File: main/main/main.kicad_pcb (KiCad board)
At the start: 2 copper layers, 50.8 x 76.2 mm, 1 part, among them U1 Teensy4.1

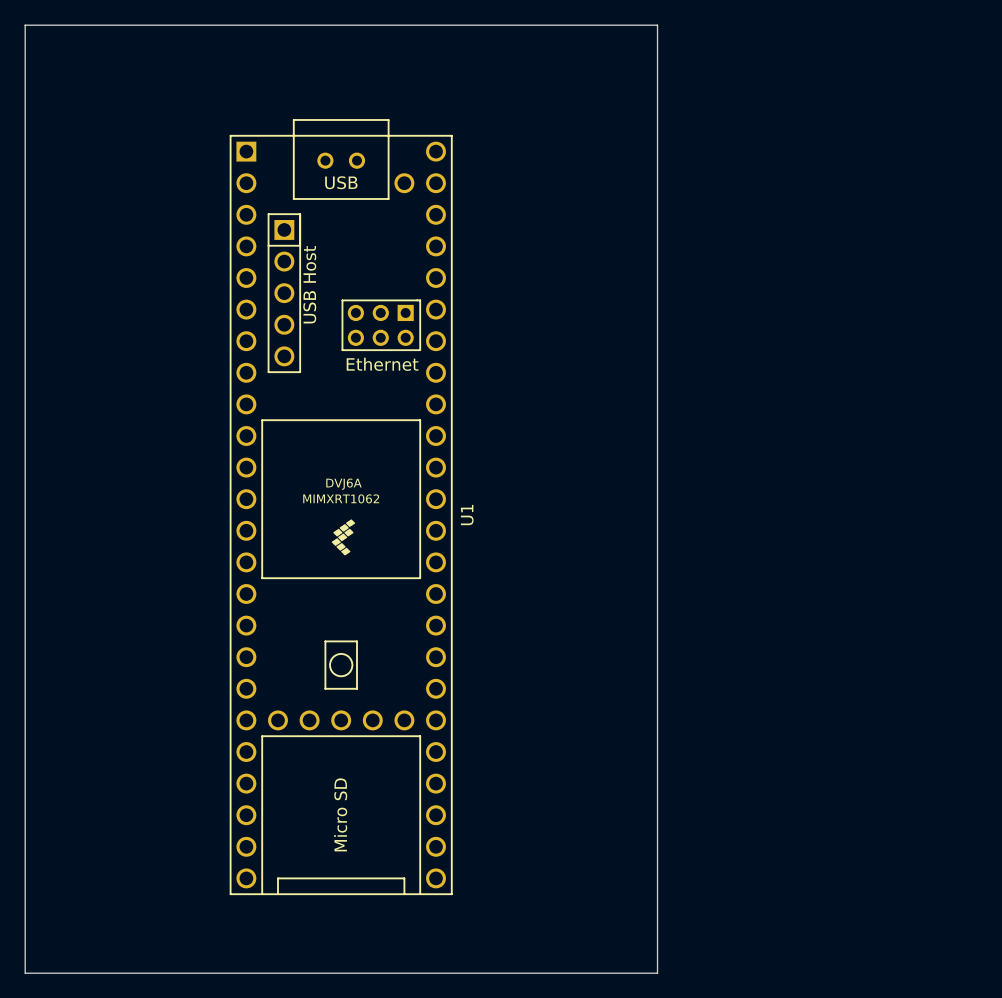
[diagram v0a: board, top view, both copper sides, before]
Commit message: working on main pcb (teensy, plugs, encoder traces)
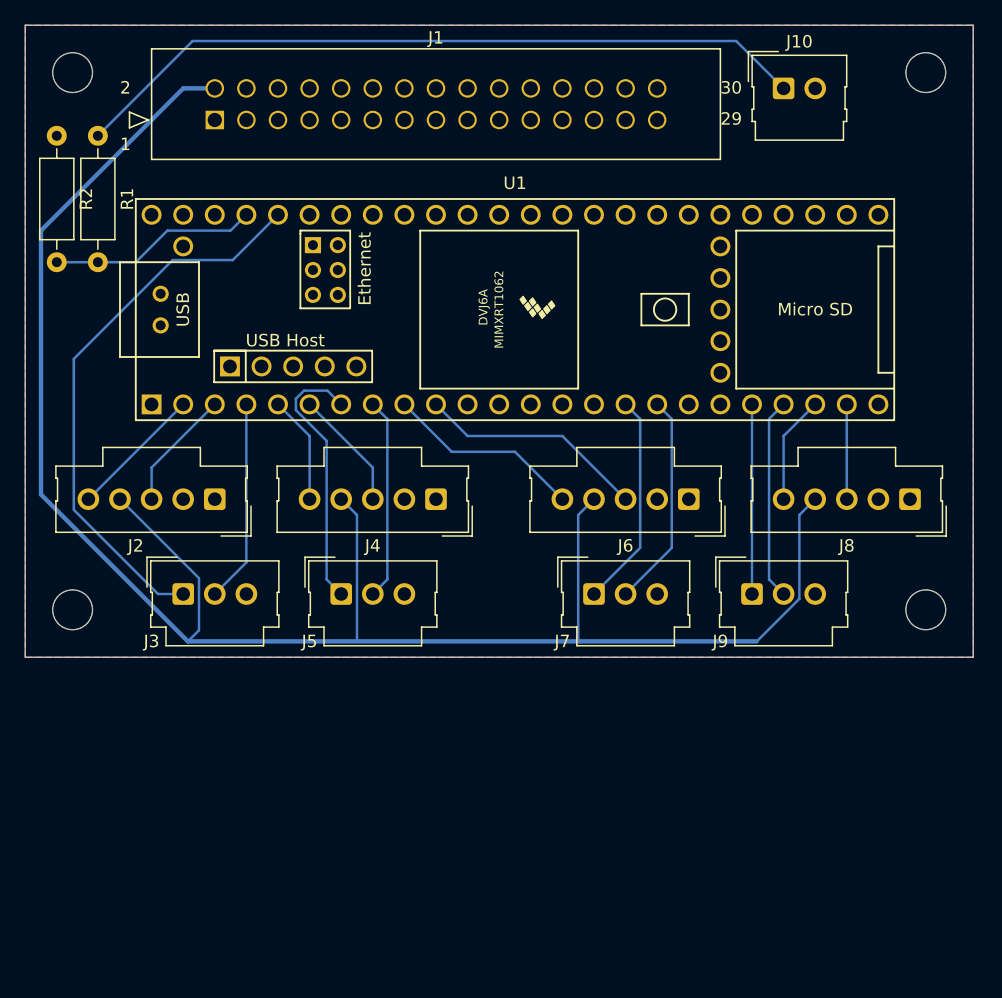
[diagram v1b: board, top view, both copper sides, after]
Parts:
- added J1: Molex2x15, projlib:CON_702463001_MOL_molex2x15, F.Cu at (116.8, 58.4)
- added J10: molex_01x02, projlib:Molex_SL_171971-0002_1x02_P2.54mm_Vertical, F.Cu at (162.6, 55.9)
- added J2: molex5P, projlib:Molex_SL_171971-0005_1x05_P2.54mm_Vertical, F.Cu at (116.8, 88.9)
- added J3: molex3P, projlib:Molex_SL_171971-0003_1x03_P2.54mm_Vertical, F.Cu at (114.3, 96.5)
- added J4: molex5P, projlib:Molex_SL_171971-0005_1x05_P2.54mm_Vertical, F.Cu at (134.6, 88.9)
- added J5: molex3P, projlib:Molex_SL_171971-0003_1x03_P2.54mm_Vertical, F.Cu at (127.0, 96.5)
- added J6: molex5P, projlib:Molex_SL_171971-0005_1x05_P2.54mm_Vertical, F.Cu at (154.9, 88.9)
- added J7: molex3P, projlib:Molex_SL_171971-0003_1x03_P2.54mm_Vertical, F.Cu at (147.3, 96.5)
- added J8: molex5P, projlib:Molex_SL_171971-0005_1x05_P2.54mm_Vertical, F.Cu at (172.7, 88.9)
- added J9: molex3P, projlib:Molex_SL_171971-0003_1x03_P2.54mm_Vertical, F.Cu at (160.0, 96.5)
- added R1: R, Resistor_THT:R_Axial_DIN0207_L6.3mm_D2.5mm_P10.16mm_Horizontal, F.Cu at (107.4, 59.7)
- added R2: R, Resistor_THT:R_Axial_DIN0207_L6.3mm_D2.5mm_P10.16mm_Horizontal, F.Cu at (104.1, 59.7)
- added REF**: MountingHole_3.2mm_M3, MountingHole:MountingHole_3.2mm_M3, F.Cu at (174.0, 54.6)
- added REF**: MountingHole_3.2mm_M3, MountingHole:MountingHole_3.2mm_M3, F.Cu at (105.4, 54.6)
- added REF**: MountingHole_3.2mm_M3, MountingHole:MountingHole_3.2mm_M3, F.Cu at (174.0, 97.8)
- added REF**: MountingHole_3.2mm_M3, MountingHole:MountingHole_3.2mm_M3, F.Cu at (105.4, 97.8)
- moved U1 21.6 mm to (141.0, 73.7), turned to 0 degrees
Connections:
- U1 pad 1: unconnected-(U1-GND-Pad1) -> GND
- U1 pad 10: unconnected-(U1-8_TX2_IN1-Pad10) -> Net-(J6-Pin_3)
- U1 pad 16: unconnected-(U1-24_A10_TX6_SCL2-Pad16) -> Net-(J7-Pin_1)
- U1 pad 17: unconnected-(U1-25_A11_RX6_SDA2-Pad17) -> Net-(J7-Pin_2)
- U1 pad 2: unconnected-(U1-0_RX1_CRX2_CS1-Pad2) -> Net-(J2-Pin_5)
- U1 pad 20: unconnected-(U1-28_RX7-Pad20) -> Net-(J9-Pin_1)
- U1 pad 21: unconnected-(U1-29_TX7-Pad21) -> Net-(J9-Pin_2)
- U1 pad 22: unconnected-(U1-30_CRX3-Pad22) -> Net-(J8-Pin_5)
- U1 pad 23: unconnected-(U1-31_CTX3-Pad23) -> Net-(J8-Pin_3)
- U1 pad 3: unconnected-(U1-1_TX1_CTX2_MISO1-Pad3) -> Net-(J2-Pin_3)
- U1 pad 4: unconnected-(U1-2_OUT2-Pad4) -> Net-(J3-Pin_2)
- U1 pad 44: unconnected-(U1-22_A8_CTX1-Pad44) -> Net-(J3-Pin_1)
- U1 pad 45: unconnected-(U1-23_A9_CRX1_MCLK1-Pad45) -> Net-(U1-23_A9_CRX1_MCLK1)
- U1 pad 47: unconnected-(U1-GND-Pad47) -> GND
- U1 pad 5: unconnected-(U1-3_LRCLK2-Pad5) -> Net-(J4-Pin_5)
- U1 pad 6: unconnected-(U1-4_BCLK2-Pad6) -> Net-(J4-Pin_3)
- U1 pad 7: unconnected-(U1-5_IN2-Pad7) -> Net-(J5-Pin_1)
- U1 pad 8: unconnected-(U1-6_OUT1D-Pad8) -> Net-(J5-Pin_2)
- U1 pad 9: unconnected-(U1-7_RX2_OUT1A-Pad9) -> Net-(J6-Pin_5)
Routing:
- net 3.3V_control: track 0.00 -> 154.1 mm
- net vbat: track 0.00 -> 59.9 mm
- net Net-(J3-Pin_1): track 0.00 -> 44.9 mm
- net Net-(J5-Pin_1): track 0.00 -> 21.6 mm
- net Net-(J6-Pin_3): track 0.00 -> 18.4 mm
- net Net-(J7-Pin_1): track 0.00 -> 17.3 mm
- net Net-(J7-Pin_2): track 0.00 -> 17.3 mm
- net Net-(U1-23_A9_CRX1_MCLK1): track 0.00 -> 16.8 mm
- net Net-(J3-Pin_2): track 0.00 -> 16.3 mm
- net Net-(J9-Pin_2): track 0.00 -> 16.2 mm
- net Net-(J5-Pin_2): track 0.00 -> 16.2 mm
- net Net-(J6-Pin_5): track 0.00 -> 15.9 mm
- net Net-(J9-Pin_1): track 0.00 -> 15.2 mm
- net Net-(J2-Pin_5): track 0.00 -> 10.8 mm
- net Net-(J4-Pin_3): track 0.00 -> 9.72 mm
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- added copper zone on F.Cu, net GND
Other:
- board size 50.8 x 76.2 mm -> 76.2 x 50.8 mm

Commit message: working on control pcb
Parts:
- added U2: ~, projlib:pololu4085, F.Cu at (105.4, 67.9)
- moved R2 74.7 mm to (175.3, 82.5), turned to 90 degrees
- moved R1 67.8 mm to (175.3, 59.7)
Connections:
- J1 pad 1: unconnected-(J1-Pin_1-Pad1) -> GND
- J1 pad 2: 3.3V_control -> vbat
- J2 pad 4: 3.3V_control -> 3.3v_encoder
- J4 pad 4: 3.3V_control -> 3.3v_encoder
- J6 pad 4: 3.3V_control -> 3.3v_encoder
- J8 pad 4: 3.3V_control -> 3.3v_encoder
- R1 pad 2: Net-(U1-23_A9_CRX1_MCLK1) -> Net-(U1-38_CS1_IN1)
- R2 pad 2: Net-(U1-23_A9_CRX1_MCLK1) -> Net-(U1-38_CS1_IN1)
- U1 pad 30: unconnected-(U1-38_CS1_IN1-Pad30) -> Net-(U1-38_CS1_IN1)
- U1 pad 45: Net-(U1-23_A9_CRX1_MCLK1) -> unconnected-(U1-23_A9_CRX1_MCLK1-Pad45)
- U1 pad 46: unconnected-(U1-3V3-Pad46) -> 3.3v_encoder
- U1 pad 48: unconnected-(U1-VIN-Pad48) -> Net-(U1-VIN)
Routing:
- net 3.3V_control: track 154.1 -> 0.00 mm
- net 3.3v_encoder: track 0.00 -> 142.8 mm
- net Net-(U1-38_CS1_IN1): track 0.00 -> 21.9 mm
- net vbat: track 59.9 -> 80.5 mm
- net Net-(U1-23_A9_CRX1_MCLK1): track 16.8 -> 0.00 mm
- net Net-(U1-VIN): track 0.00 -> 7.62 mm
- net Net-(J3-Pin_1): track 44.9 -> 43.0 mm
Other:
- board text added: "WayWayWay"

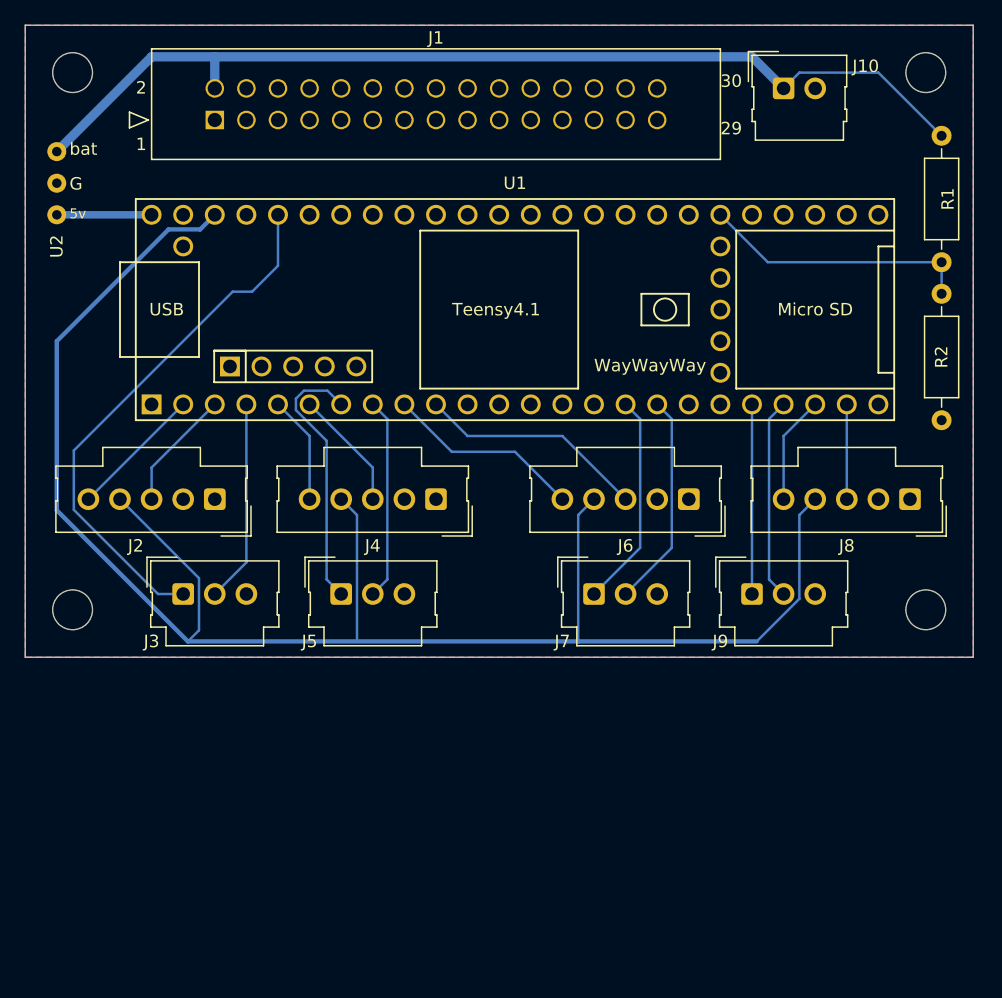
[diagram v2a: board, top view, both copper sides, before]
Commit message: add joystick plug, adjust resistors
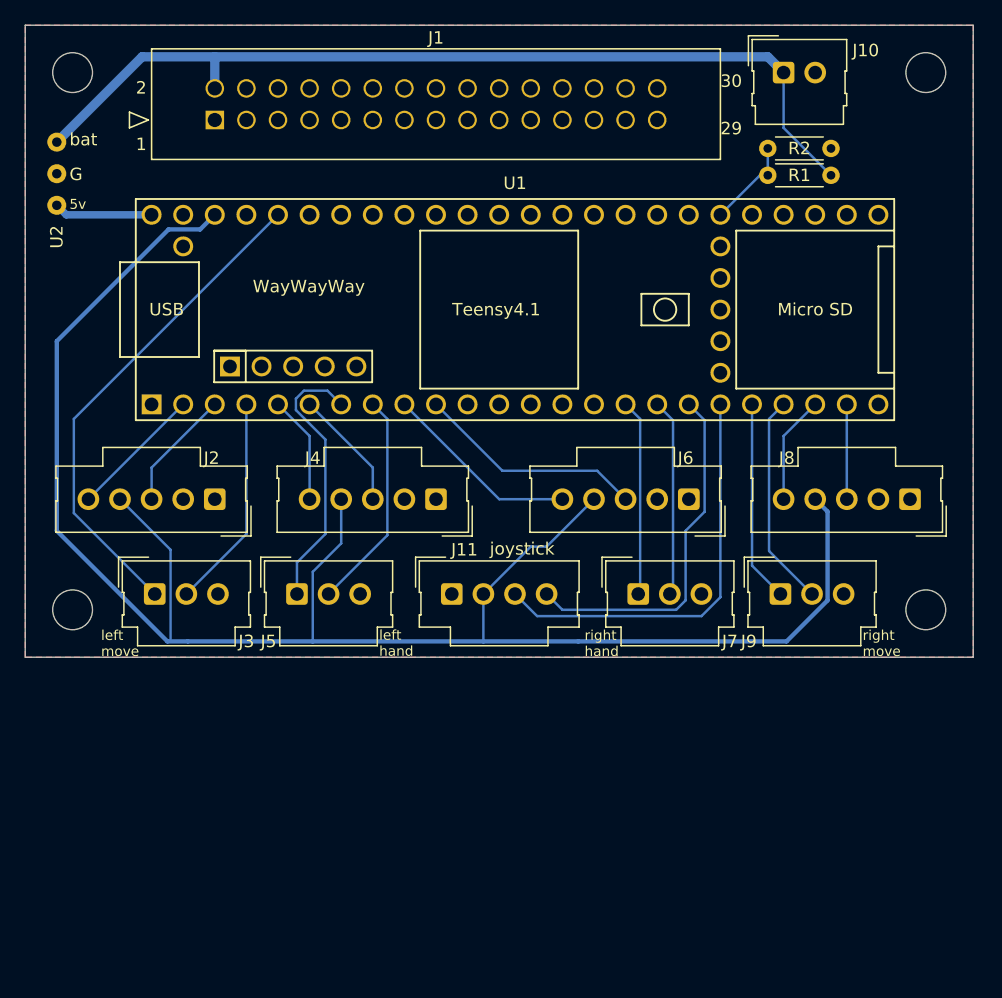
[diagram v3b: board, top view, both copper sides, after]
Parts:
- added J11: Conn_01x04, projlib:Molex_SL_171971-0004_1x04_P2.54mm_Vertical, F.Cu at (135.9, 96.5)
- R1, R2: footprint Resistor_THT:R_Axial_DIN0207_L6.3mm_D2.5mm_P10.16mm_Horizontal -> Resistor_THT:R_Axial_DIN0204_L3.6mm_D1.6mm_P5.08mm_Horizontal
- moved R2 23.6 mm to (166.4, 60.7), turned to 180 degrees
- moved R1 9.44 mm to (166.4, 62.9), turned to 180 degrees
- moved J7 3.56 mm to (150.9, 96.5)
- moved J5 3.56 mm to (123.4, 96.5)
- moved J3 2.29 mm to (112.0, 96.5)
- moved J9 2.29 mm to (162.3, 96.5)
- moved J10 1.27 mm to (162.6, 54.6)
- moved U2 0.76 mm to (105.4, 67.2)
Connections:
- U1 pad 18: unconnected-(U1-26_A12_MOSI1-Pad18) -> Net-(J11-Pin_4)
- U1 pad 19: unconnected-(U1-27_A13_SCK1-Pad19) -> Net-(J11-Pin_3)
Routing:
- net Net-(J11-Pin_3): track 0.00 -> 33.4 mm
- net Net-(J11-Pin_4): track 0.00 -> 28.9 mm
- net Net-(U1-38_CS1_IN1): track 21.9 -> 7.28 mm
- net 3.3v_encoder: track 142.8 -> 150.4 mm
- net vbat: track 80.5 -> 74.2 mm
- net Net-(J3-Pin_1): track 43.0 -> 40.0 mm
- net Net-(J7-Pin_1): track 17.3 -> 15.8 mm
- net Net-(J5-Pin_2): track 16.2 -> 17.7 mm
- net Net-(J7-Pin_2): track 17.3 -> 15.9 mm
- net Net-(J9-Pin_2): track 16.2 -> 17.2 mm
- net Net-(J3-Pin_2): track 16.3 -> 17.2 mm
- net Net-(J9-Pin_1): track 15.2 -> 16.2 mm
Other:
- board text added: "joystick"
- board text added: "left hand"
- board text added: "left move"
- board text added: "right hand"
- board text added: "right move"

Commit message: main fully routed
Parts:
- added BT1: Battery_Cell, TestPoint:TestPoint_2Pads_Pitch2.54mm_Drill0.8mm, F.Cu at (175.3, 71.1)
- added J12: Conn_02x03, Connector_PinHeader_2.54mm:PinHeader_2x03_P2.54mm_Horizontal, F.Cu at (120.0, 69.3)
- added TP1: TestPoint, TestPoint:TestPoint_2Pads_Pitch2.54mm_Drill0.8mm, F.Cu at (175.3, 78.7)
- moved R2 2.29 mm to (166.4, 63.0)
- moved R1 2.16 mm to (166.4, 60.7)
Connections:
- J1 pad 10: unconnected-(J1-Pin_10-Pad10) -> Net-(J1-Pin_10)
- J1 pad 11: unconnected-(J1-Pin_11-Pad11) -> Net-(J1-Pin_11)
- J1 pad 12: unconnected-(J1-Pin_12-Pad12) -> Net-(J1-Pin_12)
- J1 pad 13: unconnected-(J1-Pin_13-Pad13) -> Net-(J1-Pin_13)
- J1 pad 14: unconnected-(J1-Pin_14-Pad14) -> Net-(J1-Pin_14)
- J1 pad 15: unconnected-(J1-Pin_15-Pad15) -> Net-(J1-Pin_15)
- J1 pad 16: unconnected-(J1-Pin_16-Pad16) -> Net-(J1-Pin_16)
- J1 pad 17: unconnected-(J1-Pin_17-Pad17) -> Net-(J1-Pin_17)
- J1 pad 18: unconnected-(J1-Pin_18-Pad18) -> Net-(J1-Pin_18)
- J1 pad 19: unconnected-(J1-Pin_19-Pad19) -> Net-(J1-Pin_19)
- J1 pad 20: unconnected-(J1-Pin_20-Pad20) -> Net-(J1-Pin_20)
- J1 pad 21: unconnected-(J1-Pin_21-Pad21) -> Net-(J1-Pin_21)
- J1 pad 22: unconnected-(J1-Pin_22-Pad22) -> Net-(J1-Pin_22)
- J1 pad 23: unconnected-(J1-Pin_23-Pad23) -> Net-(J1-Pin_23)
- J1 pad 24: unconnected-(J1-Pin_24-Pad24) -> Net-(J1-Pin_24)
- J1 pad 25: unconnected-(J1-Pin_25-Pad25) -> Net-(J1-Pin_25)
- J1 pad 26: unconnected-(J1-Pin_26-Pad26) -> vbat
- J1 pad 27: unconnected-(J1-Pin_27-Pad27) -> Net-(J1-Pin_27)
- J1 pad 28: unconnected-(J1-Pin_28-Pad28) -> Net-(J1-Pin_28)
- J1 pad 29: unconnected-(J1-Pin_29-Pad29) -> Net-(J1-Pin_29)
- J1 pad 3: unconnected-(J1-Pin_3-Pad3) -> Net-(J1-Pin_3)
- J1 pad 30: unconnected-(J1-Pin_30-Pad30) -> Net-(J1-Pin_30)
- J1 pad 4: unconnected-(J1-Pin_4-Pad4) -> Net-(J1-Pin_4)
- J1 pad 5: unconnected-(J1-Pin_5-Pad5) -> Net-(J1-Pin_5)
- J1 pad 6: unconnected-(J1-Pin_6-Pad6) -> Net-(J1-Pin_6)
- J1 pad 7: unconnected-(J1-Pin_7-Pad7) -> Net-(J1-Pin_7)
- J1 pad 8: unconnected-(J1-Pin_8-Pad8) -> Net-(J1-Pin_8)
- J1 pad 9: unconnected-(J1-Pin_9-Pad9) -> Net-(J1-Pin_9)
- U1 pad 11: unconnected-(U1-9_OUT1C-Pad11) -> Net-(J3-Pin_1)
- U1 pad 12: unconnected-(U1-10_CS_MQSR-Pad12) -> Net-(J1-Pin_16)
- U1 pad 13: unconnected-(U1-11_MOSI_CTX1-Pad13) -> Net-(J1-Pin_18)
- U1 pad 14: unconnected-(U1-12_MISO_MQSL-Pad14) -> Net-(J1-Pin_20)
- U1 pad 15: unconnected-(U1-3V3-Pad15) -> 3.3v_encoder
- U1 pad 20: Net-(J9-Pin_1) -> Net-(U1-28_RX7)
- U1 pad 24: unconnected-(U1-32_OUT1B-Pad24) -> Net-(J9-Pin_1)
- U1 pad 25: unconnected-(U1-33_MCLK2-Pad25) -> Net-(J1-Pin_28)
- U1 pad 26: unconnected-(U1-34_RX8-Pad26) -> Net-(J1-Pin_27)
- U1 pad 27: unconnected-(U1-35_TX8-Pad27) -> Net-(J1-Pin_25)
- U1 pad 28: unconnected-(U1-36_CS-Pad28) -> Net-(J1-Pin_30)
- U1 pad 29: unconnected-(U1-37_CS-Pad29) -> Net-(J1-Pin_29)
- U1 pad 31: unconnected-(U1-39_MISO1_OUT1A-Pad31) -> Net-(J1-Pin_24)
- U1 pad 32: unconnected-(U1-40_A16-Pad32) -> Net-(J1-Pin_23)
- U1 pad 33: unconnected-(U1-41_A17-Pad33) -> Net-(J1-Pin_22)
- U1 pad 34: unconnected-(U1-GND-Pad34) -> GND
- U1 pad 36: unconnected-(U1-14_A0_TX3_SPDIF_OUT-Pad36) -> Net-(J1-Pin_21)
- U1 pad 37: unconnected-(U1-15_A1_RX3_SPDIF_IN-Pad37) -> Net-(J1-Pin_19)
- U1 pad 38: unconnected-(U1-16_A2_RX4_SCL1-Pad38) -> Net-(J1-Pin_17)
- U1 pad 39: unconnected-(U1-17_A3_TX4_SDA1-Pad39) -> Net-(J1-Pin_15)
- U1 pad 40: unconnected-(U1-18_A4_SDA-Pad40) -> Net-(J1-Pin_13)
- U1 pad 41: unconnected-(U1-19_A5_SCL-Pad41) -> Net-(J1-Pin_14)
- U1 pad 42: unconnected-(U1-20_A6_TX5_LRCLK1-Pad42) -> Net-(J1-Pin_12)
- U1 pad 43: unconnected-(U1-21_A7_RX5_BCLK1-Pad43) -> Net-(J1-Pin_10)
- U1 pad 44: Net-(J3-Pin_1) -> Net-(J1-Pin_8)
- U1 pad 45: unconnected-(U1-23_A9_CRX1_MCLK1-Pad45) -> Net-(J1-Pin_6)
- U1 pad 46: 3.3v_encoder -> unconnected-(U1-3V3-Pad46)
- U1 pad 50: unconnected-(U1-VBAT-Pad50) -> Net-(BT1-+)
- U1 pad 52: unconnected-(U1-GND-Pad52) -> Net-(BT1--)
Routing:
- net Net-(J1-Pin_20): track 0.00 -> 27.5 mm
- net Net-(J1-Pin_18): track 0.00 -> 27.5 mm
- net Net-(J1-Pin_16): track 0.00 -> 27.5 mm
- net Net-(J1-Pin_28): track 0.00 -> 27.3 mm
- net Net-(J1-Pin_27): track 0.00 -> 25.7 mm
- net Net-(J1-Pin_4): track 0.00 -> 25.0 mm
- net 3.3v_encoder: track 150.4 -> 175.4 mm
- net Net-(J1-Pin_25): track 0.00 -> 22.3 mm
- net Net-(BT1-+): track 0.00 -> 20.9 mm
- net Net-(BT1--): track 0.00 -> 19.9 mm
- net Net-(J1-Pin_11): track 0.00 -> 18.9 mm
- net Net-(U1-28_RX7): track 0.00 -> 17.0 mm
- net Net-(J1-Pin_3): track 0.00 -> 16.9 mm
- net Net-(J1-Pin_24): track 0.00 -> 15.4 mm
- net Net-(J1-Pin_9): track 0.00 -> 15.3 mm
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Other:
- board text added: "28"
- board text added: "bat+"
- board text added: "gnd"

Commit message: change plug for extra pns
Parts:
- J12: value Conn_02x03 -> Conn_01x08; footprint Connector_PinHeader_2.54mm:PinHeader_2x03_P2.54mm_Horizontal -> projlib:PinSocket_2x04_P1.27mm_Vertical
- moved J12 39.9 mm to (159.8, 73.0), turned to 90 degrees
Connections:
- BT1 pad 2: Net-(BT1--) -> GND
- J12 pad 1: Net-(J1-Pin_5) -> Net-(J1-Pin_21)
- J12 pad 2: Net-(J1-Pin_7) -> unconnected-(J12-Pin_2-Pad2)
- J12 pad 3: Net-(J1-Pin_3) -> Net-(J1-Pin_22)
- J12 pad 4: Net-(J1-Pin_9) -> Net-(J1-Pin_18)
- J12 pad 5: Net-(J1-Pin_4) -> Net-(J1-Pin_24)
- J12 pad 6: Net-(J1-Pin_11) -> Net-(J1-Pin_17)
- U1 pad 12: Net-(J1-Pin_16) -> Net-(J1-Pin_8)
- U1 pad 13: Net-(J1-Pin_18) -> Net-(J1-Pin_11)
- U1 pad 14: Net-(J1-Pin_20) -> Net-(J1-Pin_13)
- U1 pad 31: Net-(J1-Pin_24) -> Net-(J1-Pin_23)
- U1 pad 32: Net-(J1-Pin_23) -> Net-(J1-Pin_20)
- U1 pad 33: Net-(J1-Pin_22) -> Net-(J1-Pin_19)
- U1 pad 36: Net-(J1-Pin_21) -> Net-(J1-Pin_16)
- U1 pad 37: Net-(J1-Pin_19) -> Net-(J1-Pin_14)
- U1 pad 38: Net-(J1-Pin_17) -> Net-(J1-Pin_12)
- U1 pad 39: Net-(J1-Pin_15) -> Net-(J1-Pin_10)
- U1 pad 40: Net-(J1-Pin_13) -> Net-(J1-Pin_9)
- U1 pad 41: Net-(J1-Pin_14) -> Net-(J1-Pin_7)
- U1 pad 42: Net-(J1-Pin_12) -> Net-(J1-Pin_6)
- U1 pad 43: Net-(J1-Pin_10) -> Net-(J1-Pin_5)
- U1 pad 44: Net-(J1-Pin_8) -> Net-(J1-Pin_4)
- U1 pad 45: Net-(J1-Pin_6) -> Net-(J1-Pin_3)
- U1 pad 52: Net-(BT1--) -> GND
- U1 pad 58: unconnected-(U1-GND-Pad58) -> GND
- U1 pad 59: unconnected-(U1-GND-Pad59) -> GND
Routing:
- net Net-(J1-Pin_15): track 7.62 -> 39.1 mm
- net Net-(J1-Pin_17): track 7.62 -> 33.9 mm
- net Net-(J1-Pin_8): track 11.2 -> 31.7 mm
- net Net-(J1-Pin_13): track 7.62 -> 28.1 mm
- net Net-(BT1--): track 19.9 -> 0.00 mm
- net Net-(J1-Pin_21): track 7.62 -> 25.0 mm
- net Net-(J1-Pin_22): track 13.3 -> 28.1 mm
- net Net-(J1-Pin_16): track 27.5 -> 13.3 mm
- net Net-(J1-Pin_4): track 25.0 -> 11.2 mm
- net Net-(J1-Pin_24): track 15.4 -> 27.1 mm
- net Net-(J1-Pin_20): track 27.5 -> 17.8 mm
- net Net-(J1-Pin_3): track 16.9 -> 7.62 mm
- net Net-(J1-Pin_11): track 18.9 -> 28.1 mm
- net Net-(J1-Pin_18): track 27.5 -> 34.5 mm
- net Net-(J1-Pin_19): track 7.62 -> 13.3 mm
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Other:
- board text added: "v1.0"

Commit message: final adjustments for v1.0
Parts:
- added G***: LOGO, LOGO, F.Cu at (173.5, 61.1)
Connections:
- U1 pad 10: Net-(J6-Pin_3) -> Net-(J6-Pin_5)
- U1 pad 9: Net-(J6-Pin_5) -> Net-(J6-Pin_3)
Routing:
- net 3.3v_encoder: track 175.4 -> 118.2 mm
- net Net-(J7-Pin_1): track 15.8 -> 20.1 mm
- net Net-(J11-Pin_4): track 28.9 -> 33.2 mm
- net Net-(J6-Pin_3): track 18.4 -> 22.1 mm
- net Net-(J11-Pin_3): track 33.4 -> 36.0 mm
- net Net-(J7-Pin_2): track 15.9 -> 18.5 mm
- net Net-(J6-Pin_5): track 15.9 -> 13.3 mm
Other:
- board text added: "github.com/PNW-AT/standing-frame"
